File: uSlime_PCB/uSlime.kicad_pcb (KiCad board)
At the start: 2 copper layers, 25 x 22.6 mm, 38 parts, among them CN1 X1502WR-05K-N0SN, CN2 1.25T-2AW, J1 USB_C_Receptacle_USB2.0_14P, U1 ESP32-C6-MINI-1, U2 MSK-12C02_SMD_SPDT_SWITCH, U3 AP2112K-3.3TRG1, U4 MCP73831T-2ACI/OT, U5 BNO085

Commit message: Add pics and logo
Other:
- board text removed: "Slime"
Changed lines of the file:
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@@
 		(fp_text user "*"
 			(at -1.5494 -2.601 0)
-			(unlocked yes)
 			(layer "F.SilkS")
 			(effects
@@
 			(layer "B.SilkS")
 		)
+		(fp_text user "Slime"
+			(at 2.4 -1.6 0)
+			(unlocked yes)
+			(layer "B.SilkS")
+			(effects
+				(font
+					(size 1 1)
+					(thickness 0.1)
+				)
+				(justify left bottom mirror)
+			)
+		)
 	)
 	(footprint "TestPoint:TestPoint_Pad_2.0x2.0mm"
@@
 		)
 	)
-	(gr_text "Slime"
-		(at 112.65 101.75 0)
-		(layer "B.SilkS")
-		(effects
-			(font
-				(size 1 1)
-				(thickness 0.1)
-			)
-			(justify left bottom mirror)
-		)
-	)
 	(gr_text "GND"
 		(at 113.8 107.75 0)
@@
 	)
 	(group ""
-		(members "9dda514c-80db-40c8-a13a-67292e7458c3" "aec3ae13-c7a8-4876-a015-c14a7a01fa67")
-	)
-	(group ""

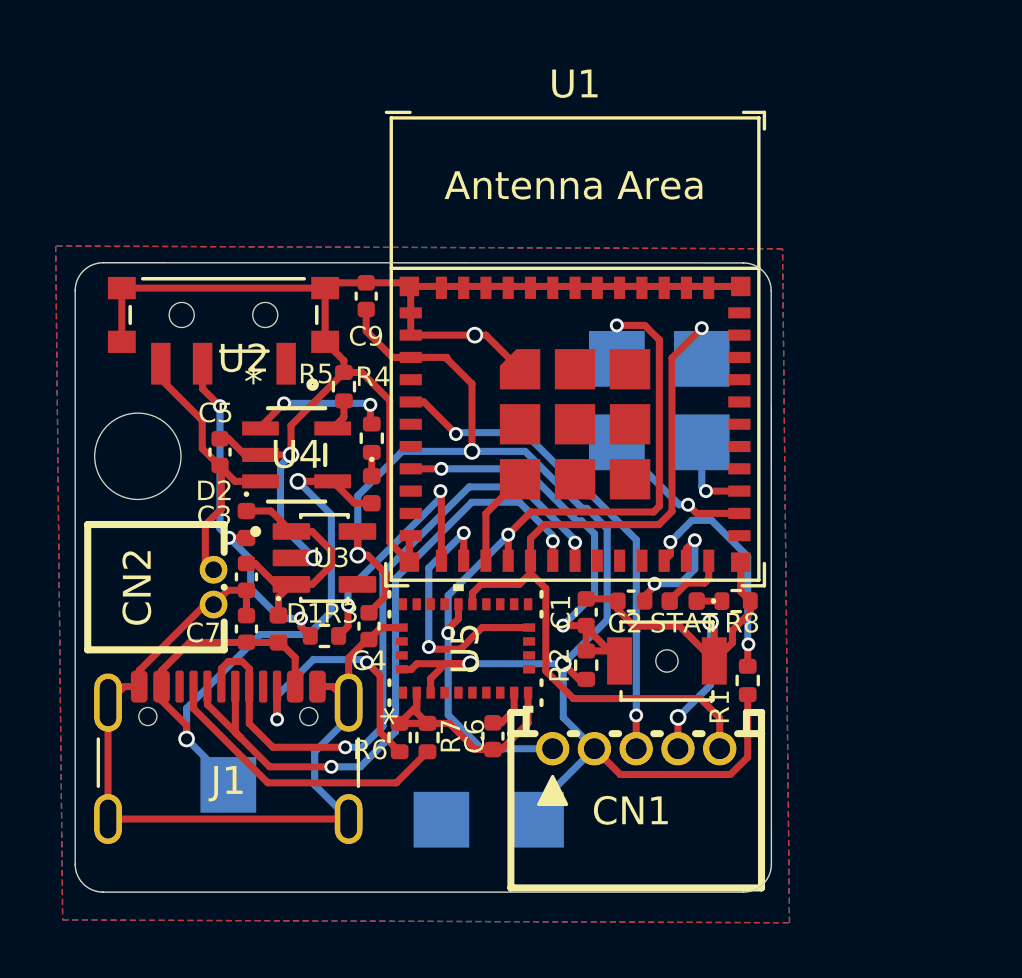
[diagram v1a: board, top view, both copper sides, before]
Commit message: Faulty BNO085 footprint
First, I do not like you UltraLibrarian anymore, for you have wasted a
lot of time and effort (and money) on footprints that are just straight
up wrong. I am this close to unleashing unbridled rage on this but will
bottle it up for now.

Second, I took the BNO085 footprint from the official SlimeVR tracker
and put it in this project. At least they have the right footprint...

Stencils for the main microcontroller does not need to change but the
extension module got a revamp in favor of being more versatile. You can
now choose which I2C address the sensor operates on; just make sure you
bridge the right contacts.
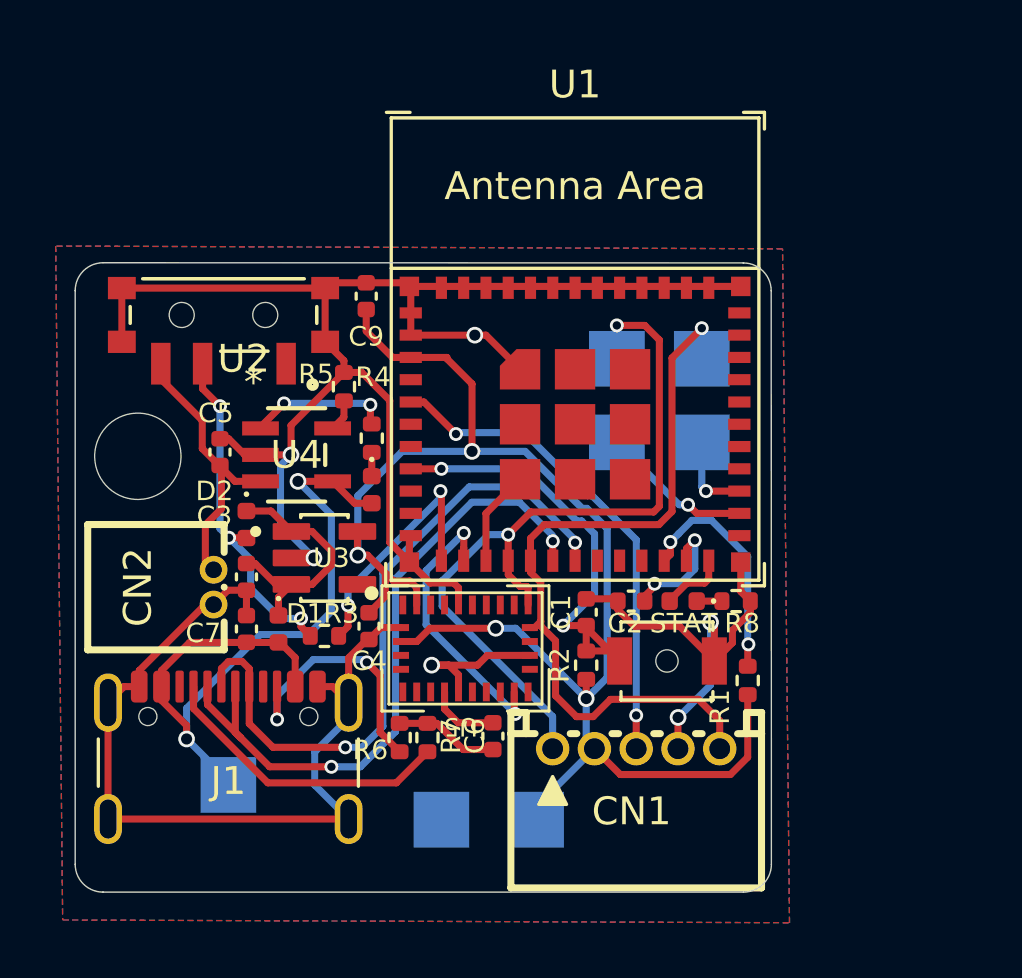
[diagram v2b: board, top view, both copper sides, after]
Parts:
- R1: value 100KOHM-0402T-1/16W-1% -> 100k
- R2: value 100KOHM-0603-1/10W-1% -> 100k
- U5: footprint uSlime-libs:LGA28_5.2X3.8_CEV -> uSlime-libs:BNO080
- turned U5 to 0 degrees
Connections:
- U5 pad 17: unconnected-(U5-SA0/H_MOSI-Pad17) -> GND
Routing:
- net GND: track 114.9 -> 117.7 mm, vias 5 -> 6
- net BNO_SCL: track 29.4 -> 27.9 mm
- net Net-(U5-CAP): track 1.58 -> 2.56 mm
- net +3.3V: track 54.4 -> 55.2 mm
- net BNO_INT: track 9.57 -> 10.2 mm
- net BNO_SDA: vias 3 -> 2

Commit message: Add version number v0.0.1a
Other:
- board text added: "v0.0.1a"
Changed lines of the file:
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@@
+		)
+	)
+	(gr_text "v0.0.1a"
+		(at 113.55 91.25 0)
+		(layer "B.SilkS")
+		(effects
+			(font
+				(size 0.7 0.7)
+				(thickness 0.1)
+			)
+			(justify mirror)
 		)
 	)

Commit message: Update main PCB schematic
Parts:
- added R10: 2.2k, Resistor_SMD:R_0402_1005Metric, F.Cu at (130.9, 103.1)
- added R11: 10k, Resistor_SMD:R_0402_1005Metric, F.Cu at (128.0, 106.6)
- added R12: 10k, Resistor_SMD:R_0402_1005Metric, F.Cu at (128.0, 108.6)
- added R9: 2.2k, Resistor_SMD:R_0402_1005Metric, F.Cu at (130.9, 101.2)
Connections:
- CN2 pad 1: VBAT -> GND
- CN2 pad 2: GND -> VBAT
- U5 pad 11: unconnected-(U5-NRST-Pad11) -> Net-(U5-NRST)
- U5 pad 17: GND -> unconnected-(U5-SA0/H_MOSI-Pad17)
- U5 pad 18: unconnected-(U5-H_CSN-Pad18) -> GND
- U5 pad 4: unconnected-(U5-BOOTN-Pad4) -> Net-(U5-BOOTN)
- U5 pad 5: unconnected-(U5-PS1-Pad5) -> GND
- U5 pad 6: unconnected-(U5-PS0/WAKE-Pad6) -> GND
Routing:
- net GND: track 117.7 -> 113.4 mm
- net VBAT: track 10.4 -> 11.6 mm

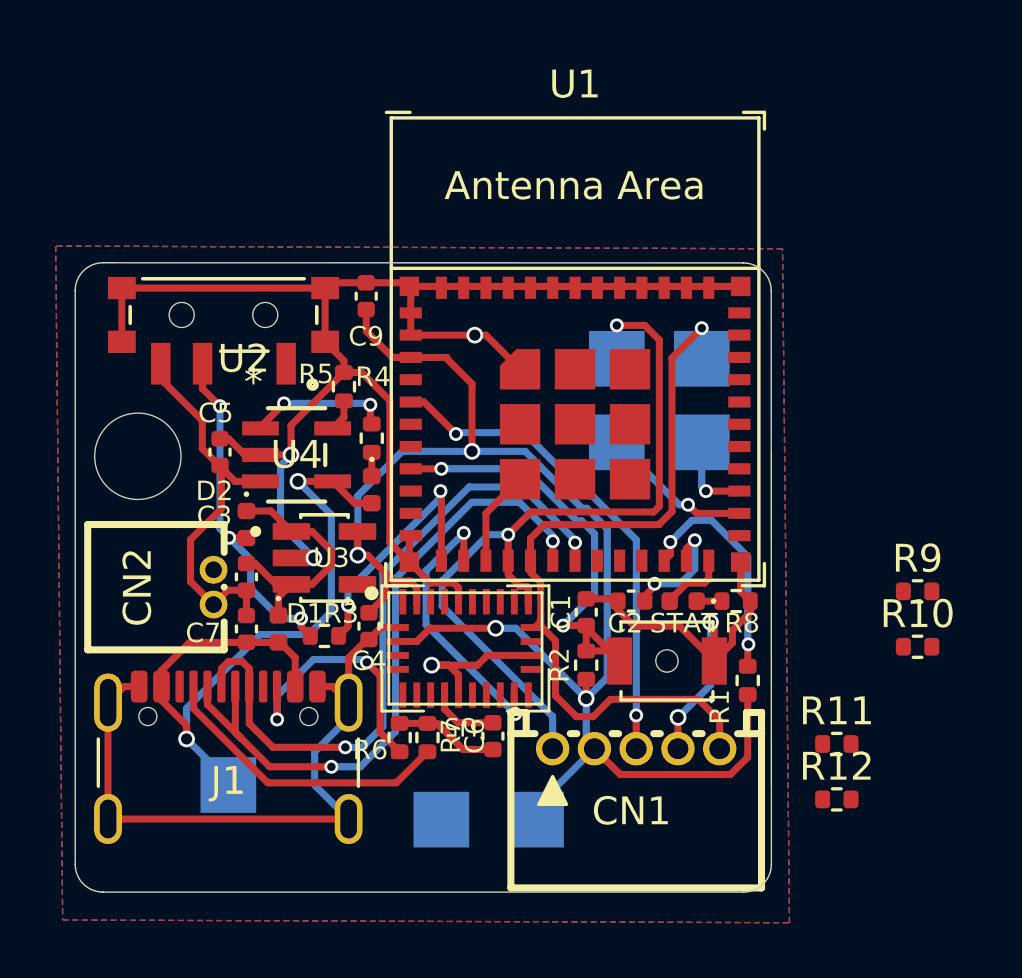
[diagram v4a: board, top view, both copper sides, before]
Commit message: v0.0.2a Modify BNO I2C
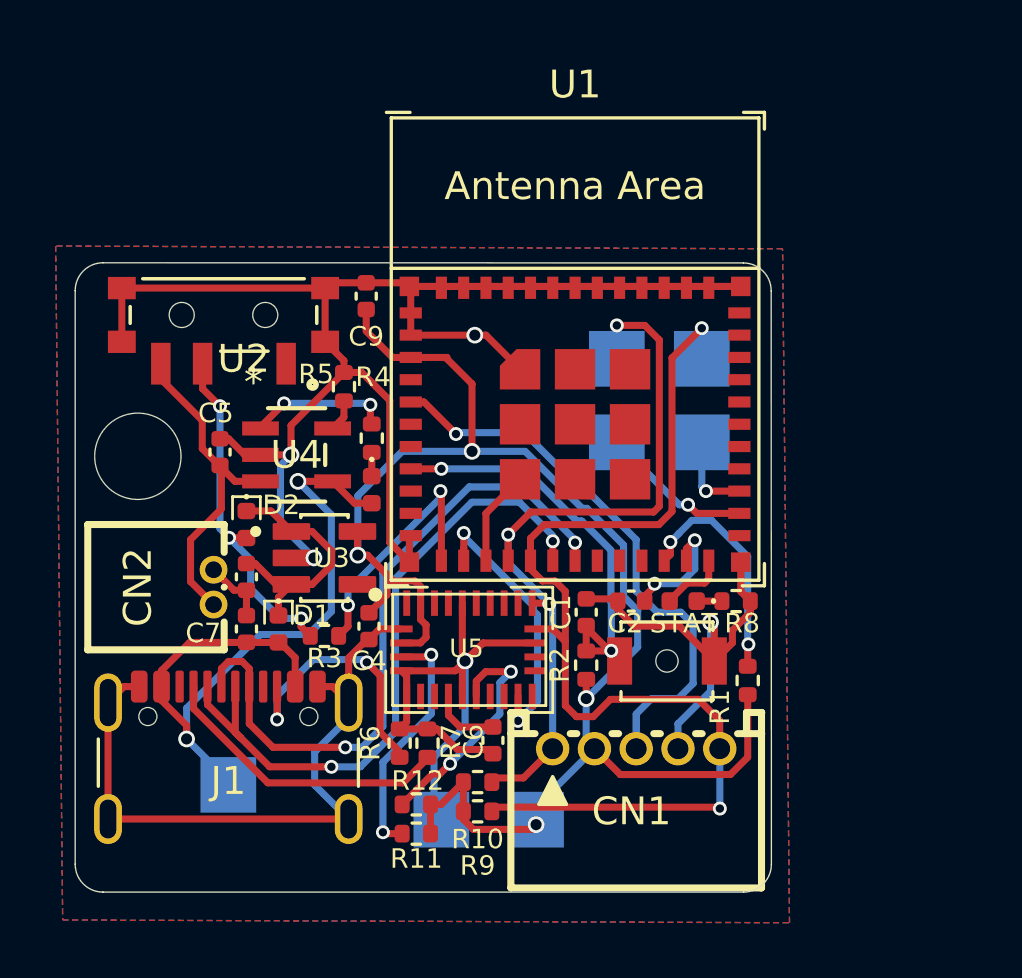
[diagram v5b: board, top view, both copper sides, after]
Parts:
- D1, D2: footprint Diode_SMD:D_0402_1005Metric -> uSlime-libs:D_0402_1005Metric
- moved R9 17.7 mm to (115.1, 109.0)
- moved R10 16.5 mm to (115.1, 108.0)
- moved R11 15.4 mm to (112.9, 109.8), turned to 180 degrees
- moved R12 15.1 mm to (112.9, 108.8)
- moved R6 0.20 mm to (112.3, 106.6)
- moved R7 0.20 mm to (113.3, 106.6)
- moved C6 0.15 mm to (115.7, 106.5)
- moved U5 0.14 mm to (114.8, 103.2)
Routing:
- net BNO_SCL: track 27.9 -> 39.3 mm, vias 1 -> 2
- net GND: track 113.4 -> 122.4 mm, vias 6 -> 5
- net Net-(U5-BOOTN): track 0.00 -> 8.91 mm, vias 0 -> 2
- net Net-(U5-NRST): track 0.00 -> 8.47 mm, vias 0 -> 2
- net BNO_INT2: track 17.7 -> 21.6 mm, vias 2 -> 1
- net +3.3V: track 55.2 -> 57.5 mm
- net BNO_SDA: track 28.5 -> 27.3 mm, vias 2 -> 3
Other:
- board text added: "v0.0.2a"
- board text removed: "v0.0.1a"

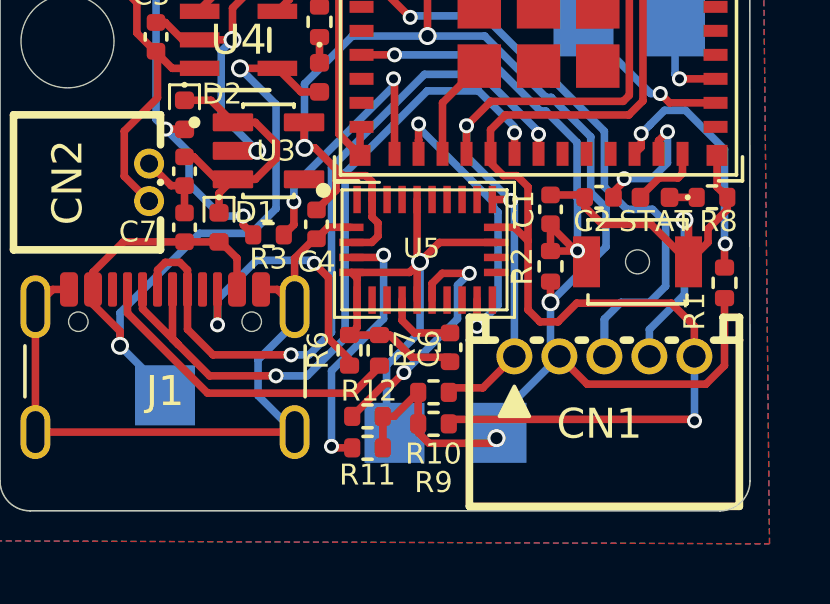
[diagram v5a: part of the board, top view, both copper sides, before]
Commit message: v0.0.3a Fix wrong I2C address for 0x4A
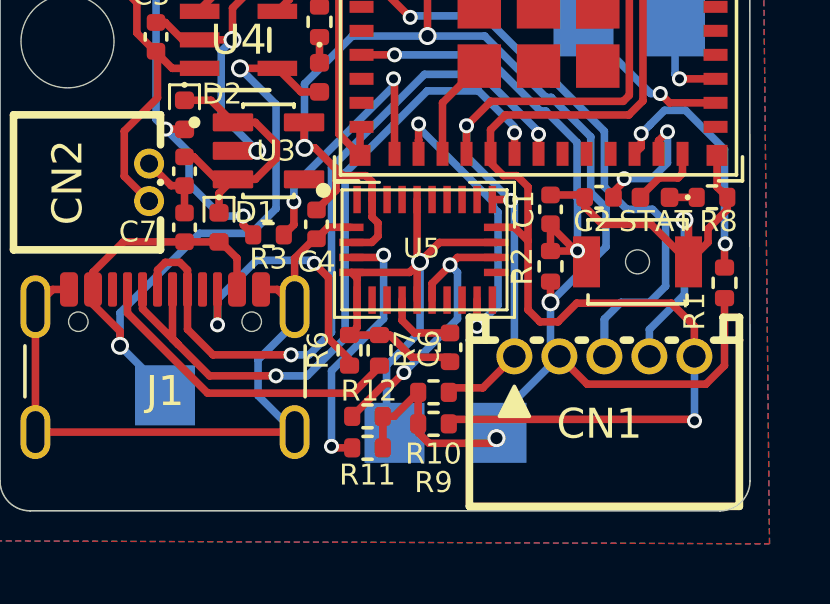
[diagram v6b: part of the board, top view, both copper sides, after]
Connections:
- R12 pad 1: Net-(U5-NRST) -> 0x4A
- U5 pad 11: Net-(U5-NRST) -> 0x4A
- U5 pad 17: unconnected-(U5-SA0/H_MOSI-Pad17) -> 0x4A
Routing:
- net 0x4A: track 0.00 -> 9.82 mm, vias 0 -> 2
- net Net-(U5-NRST): track 8.47 -> 0.00 mm, vias 2 -> 0
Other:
- board text added: "v0.0.3a"
- board text removed: "v0.0.2a"

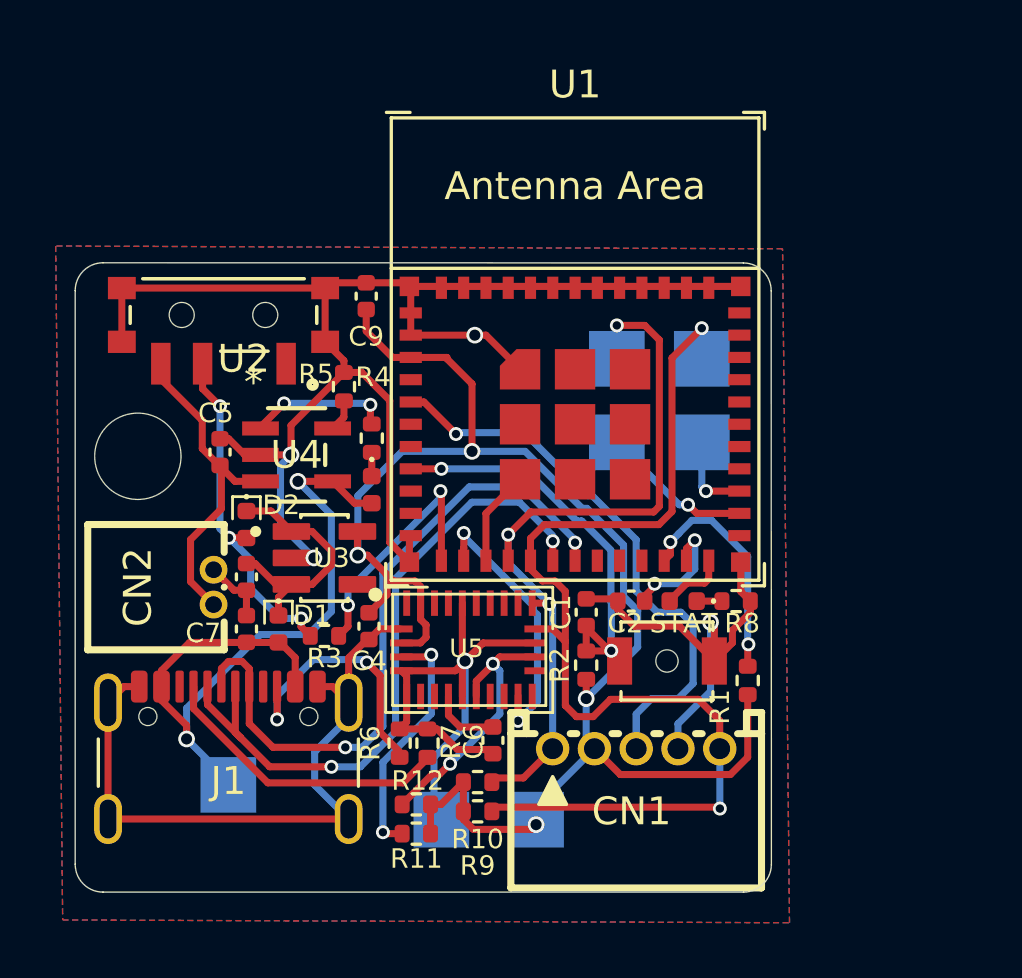
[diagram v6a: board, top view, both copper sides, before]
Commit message: Change bat sense pin to not IO0
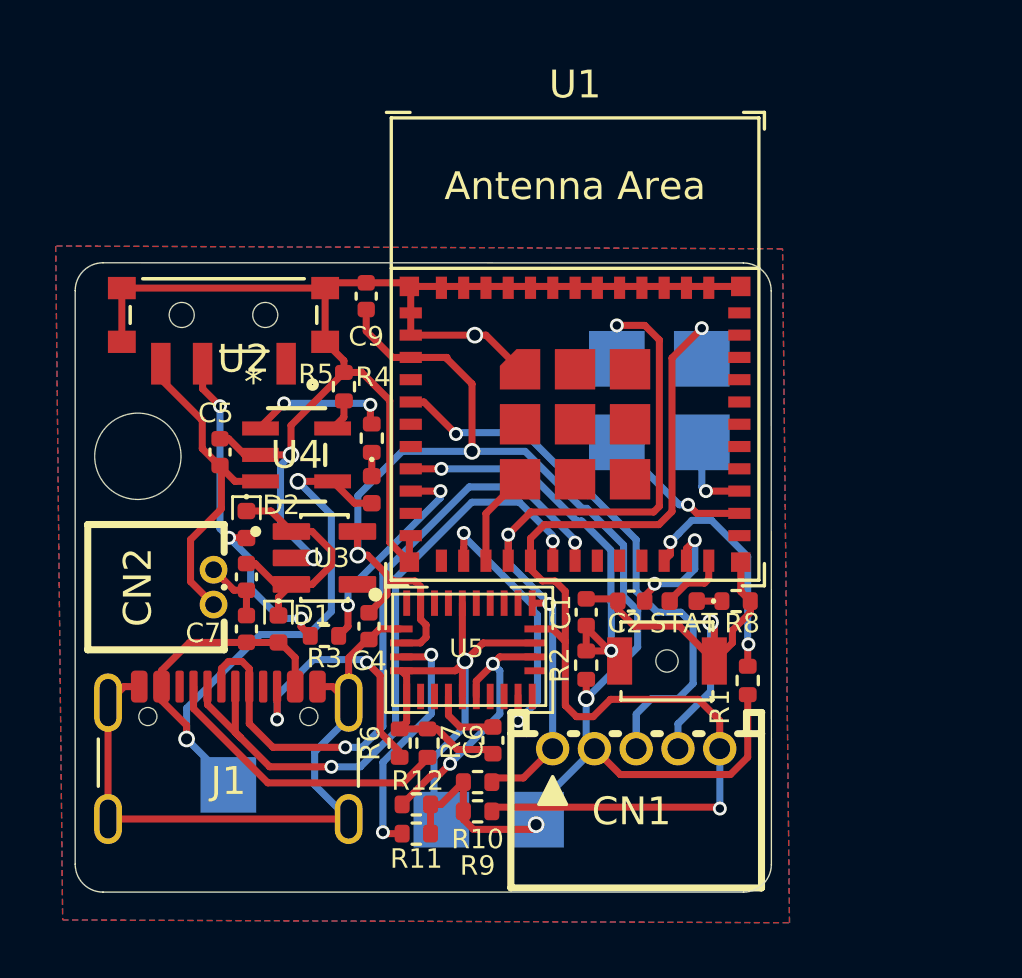
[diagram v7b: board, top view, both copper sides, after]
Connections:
- U1 pad 12: BatSense -> /ESP32-C6FH4/IO0
- U1 pad 9: /ESP32-C6FH4/IO4 -> BatSense
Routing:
- net BatSense: track 9.23 -> 7.83 mm

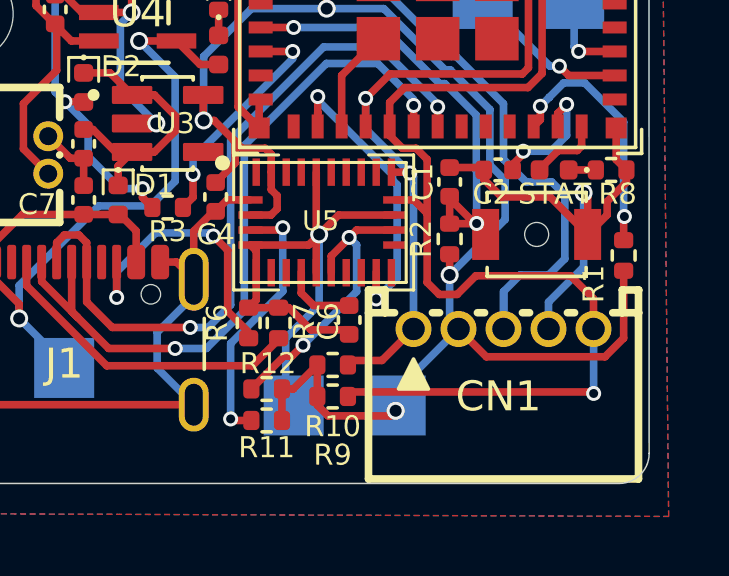
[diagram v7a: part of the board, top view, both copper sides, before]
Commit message: Connect DI without resistor
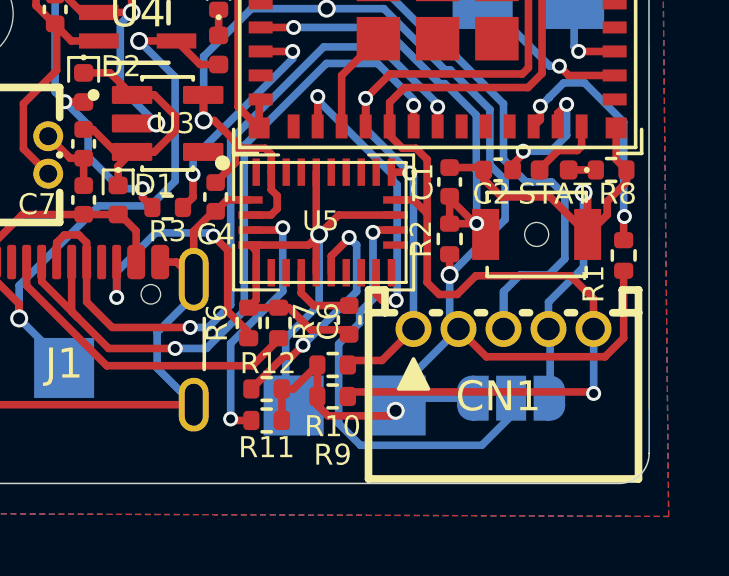
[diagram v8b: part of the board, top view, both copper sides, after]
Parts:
- added JP1: Jumper_3_Open, Jumper:SolderJumper-3_P1.3mm_Open_RoundedPad1.0x1.5mm, B.Cu at (121.0, 109.1)
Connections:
- R12 pad 1: 0x4A -> Net-(U5-NRST)
- U5 pad 11: 0x4A -> Net-(U5-NRST)
- U5 pad 17: 0x4A -> Net-(JP1-C)
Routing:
- net Net-(JP1-C): track 0.00 -> 14.7 mm, vias 0 -> 1
- net 0x4A: track 9.82 -> 0.00 mm, vias 2 -> 0
- net Net-(U5-NRST): track 0.00 -> 8.18 mm, vias 0 -> 2
- net +3.3V: track 57.5 -> 60.2 mm
- net GND: track 122.4 -> 124.8 mm
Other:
- board text added: "4A"
- board text added: "4B"
